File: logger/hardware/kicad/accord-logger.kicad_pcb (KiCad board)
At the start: 2 copper layers, 120 x 80 mm, 31 parts, among them J1 Board connector 14-way, J5 SD breakout 6-way, Q5 IPD50P04P4L-11, Q6 2N3904, Q7 2N3904, U1 RaspberryPi_Pico_W, U6 LM2678T-5.0

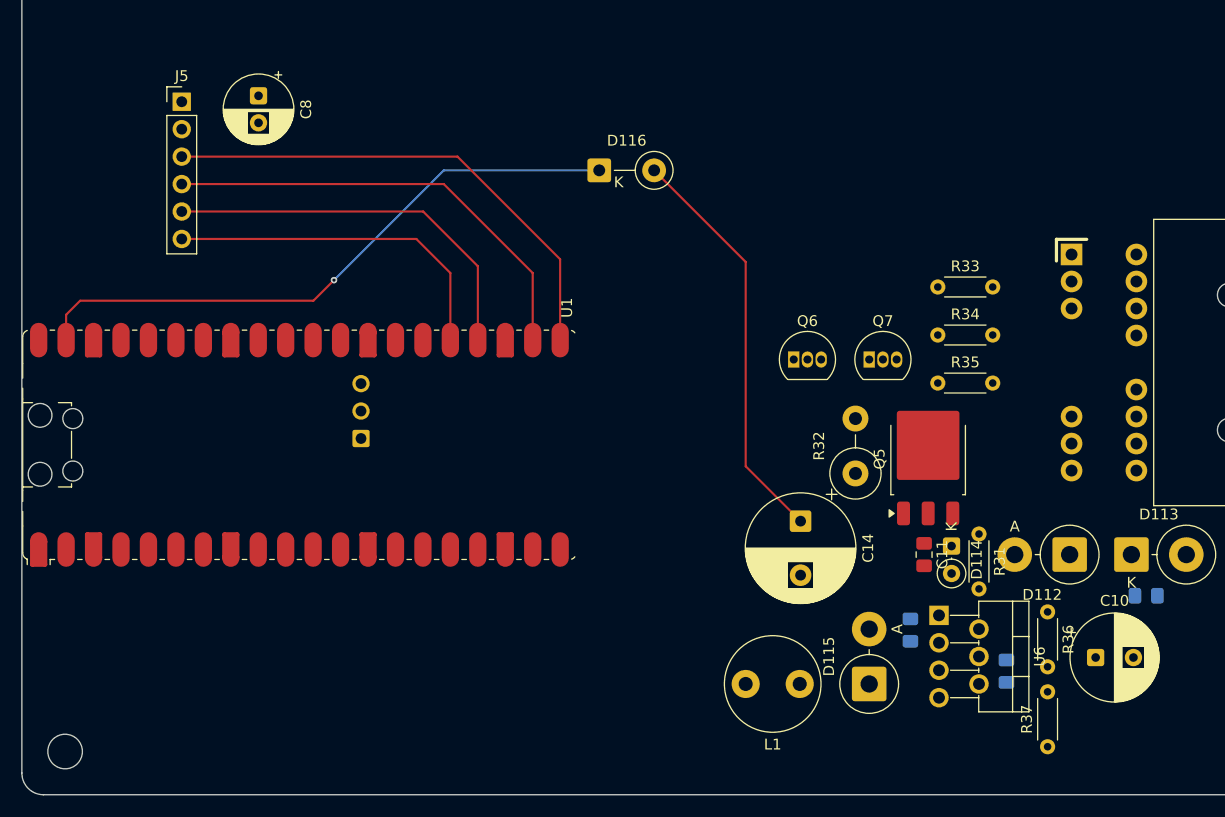
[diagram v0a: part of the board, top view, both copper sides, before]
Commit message: layout: Pico turned antenna-to-edge, buck loop tightened
Owner changes after the first review:
- U1 rotated 0 deg: antenna end at the bottom board edge, USB end inboard
  with its cable keepout clear to the top edge.
- Buck rearranged around U6 (now 90 deg): hot loop CIN -> VIN -> SW ->
  catch diode -> CIN- is 12.7 + 10.1 + 11.4 mm (was 11.1 + 9.1 + 24.6;
  keyless 9.5 + 6.5 + 22.9). L1 to SW 7.1 mm (was 14.4).
- R32/C14 courtyard overlap fixed.

Review findings (scratch-copy DRC; schematic parity: only the 39 timer
parts not yet pulled in):
- J5's drawn SD-module courtyard (B side, x 110-126, y 119-136) covers
  the Pico antenna keepout from behind.
- H4 hole edge reaches ~0.4 mm into the RF keepout; NPTH, no copper.
- C11 (CIB, VIN ceramic) is 14 mm from U6.2 (keyless C16: 3.2 mm);
  C12 (CBOOST) 12.7/10.5 mm from U6.1/U6.3 (keyless 6.2/8.7).
- C14 output bulk is ~30 mm from L1's output pad.
- 0.5 mm dangling P12 stub on B.Cu at D113.1.
- Silkscreen overlaps only otherwise.

Claude-Session-ID: 42dd0e33-28b5-4936-847e-9c2e1d2488fa
Co-Authored-By: Claude Opus 5.5 <noreply@anthropic.com>
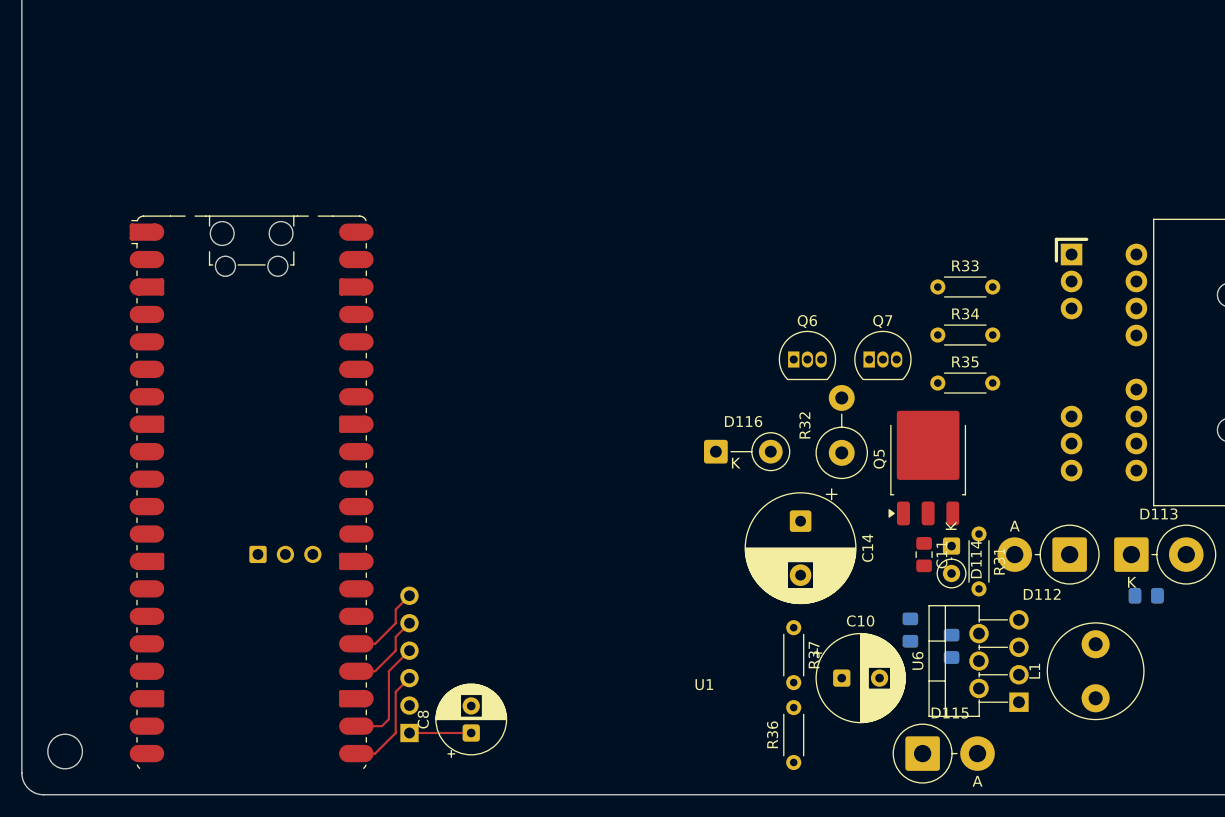
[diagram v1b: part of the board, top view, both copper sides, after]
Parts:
- J5: moved to B.Cu
- moved C8 62.2 mm to (130.2, 134.0), turned to 90 degrees
- moved J5 62.1 mm to (124.5, 134.0)
- moved D116 28.2 mm to (152.8, 108.0)
- moved L1 27.4 mm to (188.0, 130.8), turned to 90 degrees
- moved R36 27.3 mm to (160.0, 136.7), turned to 90 degrees
- moved R37 25.9 mm to (160.0, 124.2), turned to -90 degrees
- moved C10 23.6 mm to (164.5, 128.9)
- moved U6 10.9 mm to (180.9, 131.1), turned to 90 degrees
- moved D115 8.12 mm to (171.9, 135.9), turned to 0 degrees
- moved U1 6.27 mm to (109.9, 111.8), turned to 0 degrees
- moved C13 5.58 mm to (174.6, 126.0), turned to -90 degrees
- moved R32 2.29 mm to (164.5, 108.1)
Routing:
- net /VSYS: track 57.2 -> 0.00 mm, vias 1 -> 0
- net /B5: track 38.1 -> 0.00 mm
- net /SD_MISO: track 46.4 -> 10.0 mm
- net /SD_CS: track 42.1 -> 10.4 mm
- net /SD_SCK: track 36.3 -> 7.50 mm
- net /SD_MOSI: track 32.4 -> 7.50 mm
- net /P3V3_SW: track 0.00 -> 5.72 mm

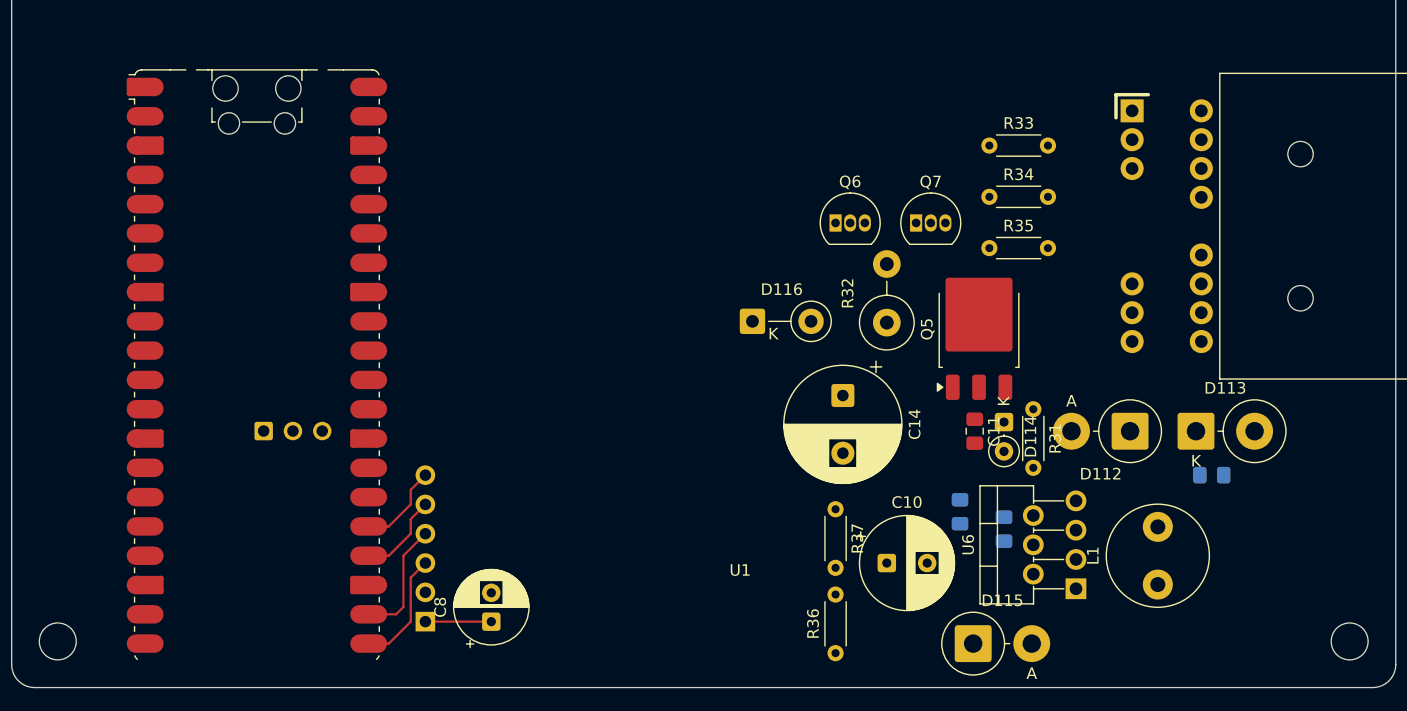
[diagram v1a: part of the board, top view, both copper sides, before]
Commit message: layout: buck bypass caps at U6, SD module beside the antenna
Owner fixes after the second review (scratch-copy DRC; only the 39 timer
parts are missing from schematic parity):
- C11 (VIN ceramic) 2.6/5.7 mm from U6.2/U6.4, was 14 (keyless 3.2).
- C12 (boost) 2.7/2.7 mm from U6.1/U6.3, was 12.7/10.5.
- C13 2.5/2.6 mm from U6.6/U6.4.
- C14 10.8 mm from L1's output, was ~30; C14- to D115 A 21.9 mm.
- J5's SD-module outline moved off the Pico antenna (now x 120.8-137.1,
  3.8 mm clear of the antenna keepout).
- Dangling P12 stub removed.
Hot loop unchanged (12.7 + 10.1 + 11.4 mm). Remaining: H4 hole edge in
the RF keepout (NPTH; use nylon hardware), silkscreen tidy-up.

Claude-Session-ID: 42dd0e33-28b5-4936-847e-9c2e1d2488fa
Co-Authored-By: Claude Opus 5.5 <noreply@anthropic.com>
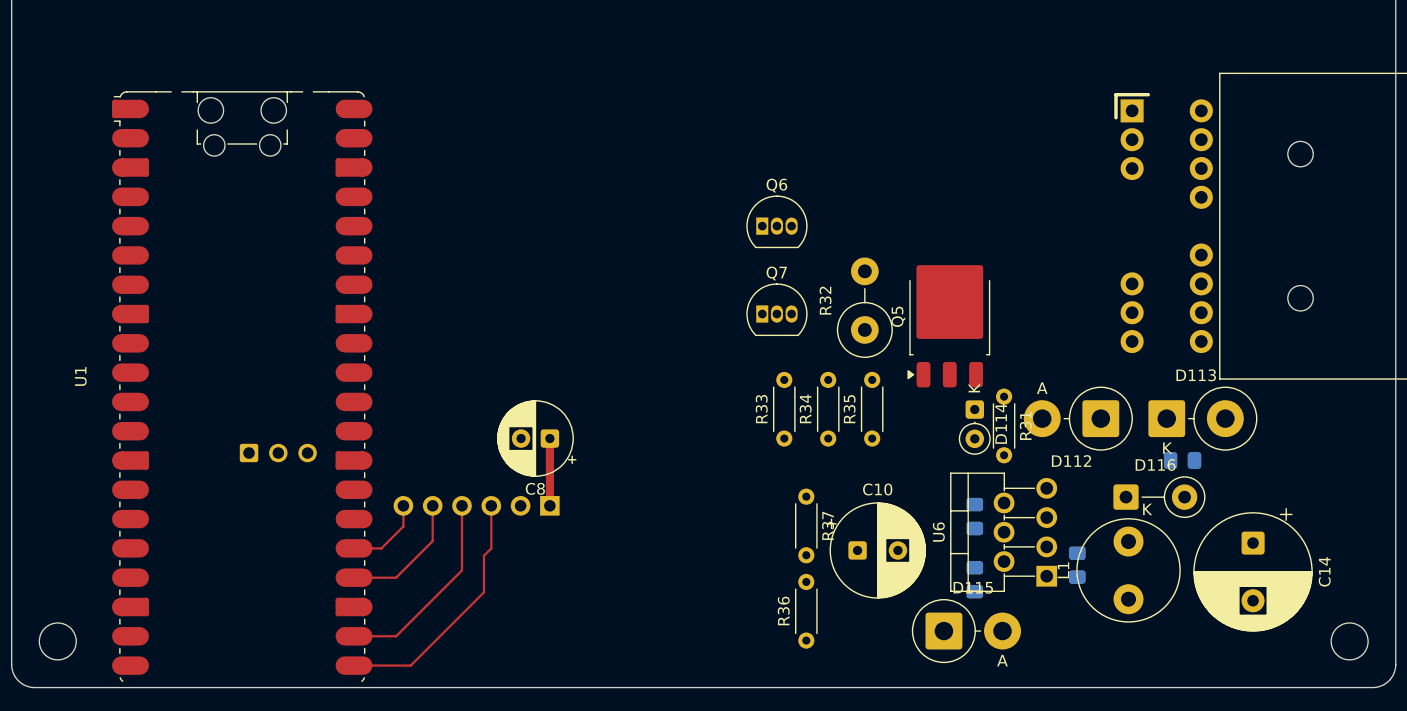
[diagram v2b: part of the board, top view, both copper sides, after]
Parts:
- C11: moved to B.Cu
- moved C14 37.8 mm to (196.2, 127.2)
- moved D116 35.8 mm to (185.2, 123.2)
- moved R33 31.0 mm to (155.6, 118.1), turned to 90 degrees
- moved R34 25.2 mm to (159.4, 118.1), turned to 90 degrees
- moved R35 19.4 mm to (163.2, 118.1), turned to 90 degrees
- moved C8 16.7 mm to (135.3, 118.1), turned to 180 degrees
- moved Q7 15.5 mm to (153.7, 107.3)
- moved J5 14.7 mm to (135.3, 123.9), turned to 90 degrees
- moved C11 12.9 mm to (172.1, 130.4)
- moved C12 11.2 mm to (181.0, 129.1), turned to 90 degrees
- moved Q6 6.36 mm to (153.7, 99.7)
- moved L1 2.84 mm to (185.4, 132.0)
- moved C9 2.84 mm to (190.1, 120.0)
- moved C10 2.76 mm to (161.9, 127.8)
- moved C13 2.76 mm to (172.1, 124.9)
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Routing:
- net /SD_MISO: track 10.0 -> 21.7 mm
- net /SD_CS: track 10.4 -> 17.3 mm
- net /SD_SCK: track 7.50 -> 11.2 mm
- net /SD_MOSI: track 7.50 -> 6.85 mm

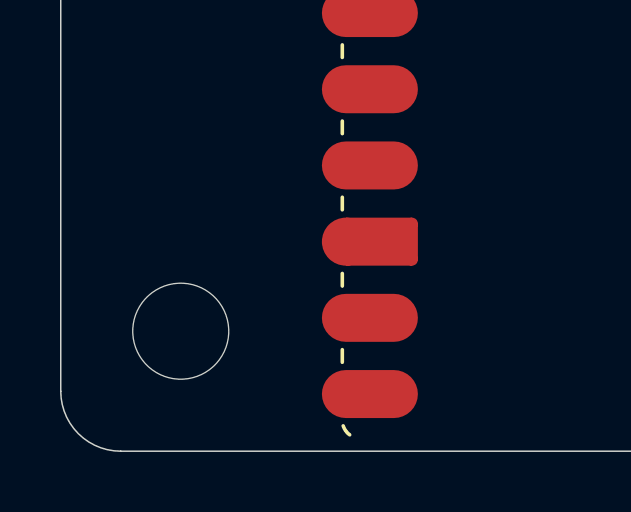
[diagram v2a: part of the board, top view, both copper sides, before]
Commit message: layout: H4 moved 1.08 mm inboard, clear of the Pico RF keepout
Hole edge now at y 136.22, the keepout starts at 136.76. H4 is no longer
4 mm from the bottom edge like H2 (134.62 vs 135.70).

Claude-Session-ID: 42dd0e33-28b5-4936-847e-9c2e1d2488fa
Co-Authored-By: Claude Opus 5.5 <noreply@anthropic.com>
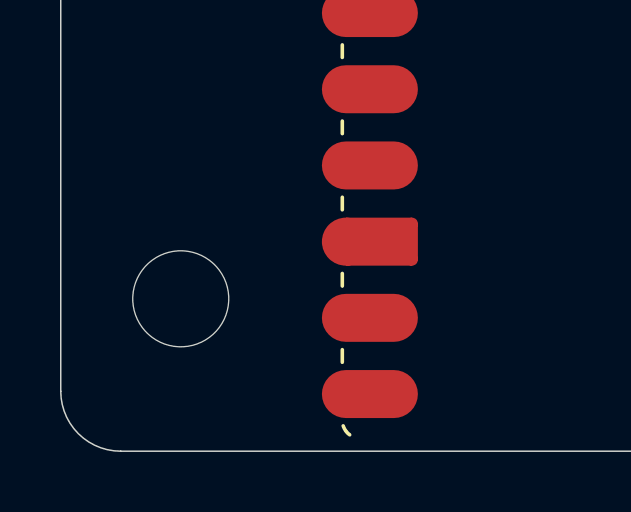
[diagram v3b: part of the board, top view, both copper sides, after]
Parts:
- moved H4 1.08 mm to (92.6, 134.6)
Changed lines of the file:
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@@
 	(footprint "MountingHole:MountingHole_3.2mm_M3"
 		(layer "F.Cu")
-		(at 92.59 135.7 -90)
+		(at 92.59 134.62 -90)
 		(descr "Mounting Hole 3.2mm, M3, no annular, generated by kicad-footprint-generator mountinghole.py")
 		(tags "mountinghole M3")

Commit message: layout: timer batch imported (39 parts, off the board edge, unplaced)
a5_supply, hold, clock and cutoff came in with "Update PCB from Schematic";
they sit to the right of the outline, x 215-270 mm. No placed footprint moved.

Claude-Session-ID: 42dd0e33-28b5-4936-847e-9c2e1d2488fa
Co-Authored-By: Claude Opus 5.5 <noreply@anthropic.com>
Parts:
- added C15: 33uF/16V, Capacitor_Tantalum_SMD:CP_EIA-7343-31_Kemet-D_HandSolder, F.Cu at (222.9, 68.6)
- added C16: 10nF, Capacitor_SMD:C_0805_2012Metric_Pad1.18x1.45mm_HandSolder, F.Cu at (247.3, 66.7)
- added C17: 100nF, Capacitor_SMD:C_0805_2012Metric_Pad1.18x1.45mm_HandSolder, F.Cu at (247.3, 71.2)
- added C18: 100nF, Capacitor_SMD:C_0805_2012Metric_Pad1.18x1.45mm_HandSolder, F.Cu at (247.3, 75.7)
- added C19: 100nF, Capacitor_SMD:C_0805_2012Metric_Pad1.18x1.45mm_HandSolder, F.Cu at (247.3, 80.0)
- added C20: 100nF, Capacitor_SMD:C_0805_2012Metric_Pad1.18x1.45mm_HandSolder, F.Cu at (247.3, 84.5)
- added C21: 100nF, Capacitor_SMD:C_0805_2012Metric_Pad1.18x1.45mm_HandSolder, F.Cu at (247.3, 88.7)
- added C22: 100nF, Capacitor_SMD:C_0805_2012Metric_Pad1.18x1.45mm_HandSolder, F.Cu at (247.3, 93.2)
- added C23: 100nF, Capacitor_SMD:C_0805_2012Metric_Pad1.18x1.45mm_HandSolder, F.Cu at (247.3, 97.7)
- added C4: 4.7uF/50V, Capacitor_SMD:C_1210_3225Metric_Pad1.33x2.70mm_HandSolder, F.Cu at (261.6, 72.4)
- added C5: 4.7uF/50V, Capacitor_SMD:C_1210_3225Metric_Pad1.33x2.70mm_HandSolder, F.Cu at (261.6, 78.7)
- added C6: 4.7uF/50V, Capacitor_SMD:C_1210_3225Metric_Pad1.33x2.70mm_HandSolder, F.Cu at (261.6, 85.1)
- added C7: 100nF, Capacitor_SMD:C_0805_2012Metric_Pad1.18x1.45mm_HandSolder, F.Cu at (247.3, 62.2)
- added D111: BZX55C22, Diode_THT:D_DO-35_SOD27_P2.54mm_Vertical_KathodeUp, F.Cu at (235.6, 85.1)
- added JP1: HOLD link, Connector_PinHeader_2.54mm:PinHeader_1x02_P2.54mm_Vertical, F.Cu at (217.2, 76.8)
- added Q8: BSS138P, Package_TO_SOT_SMD:SOT-23, F.Cu at (270.2, 74.6)
- added Q9: MMBT3904, Package_TO_SOT_SMD:SOT-23, F.Cu at (270.2, 81.4)
- added R22: 820R, Resistor_SMD:R_1206_3216Metric_Pad1.30x1.75mm_HandSolder, F.Cu at (267.0, 55.9)
- added R28: 47k, Resistor_SMD:R_0805_2012Metric_Pad1.20x1.40mm_HandSolder, F.Cu at (252.0, 62.2)
- added R29: 1k, Resistor_SMD:R_0805_2012Metric_Pad1.20x1.40mm_HandSolder, F.Cu at (252.1, 66.6)
- added R38: 1k, Resistor_SMD:R_0805_2012Metric_Pad1.20x1.40mm_HandSolder, F.Cu at (252.1, 71.1)
- added R39: 0R, Resistor_SMD:R_1206_3216Metric_Pad1.30x1.75mm_HandSolder, F.Cu at (267.0, 61.0)
- added R40: 0R, Resistor_SMD:R_1206_3216Metric_Pad1.30x1.75mm_HandSolder, F.Cu at (267.0, 66.0)
- added R41: 100k, Resistor_SMD:R_0805_2012Metric_Pad1.20x1.40mm_HandSolder, F.Cu at (252.1, 75.5)
- added R42: 1k, Resistor_SMD:R_0805_2012Metric_Pad1.20x1.40mm_HandSolder, F.Cu at (252.0, 79.7)
- added R43: 100k, Resistor_SMD:R_0805_2012Metric_Pad1.20x1.40mm_HandSolder, F.Cu at (252.0, 84.1)
- added R44: 47k, Resistor_SMD:R_0805_2012Metric_Pad1.20x1.40mm_HandSolder, F.Cu at (252.0, 88.3)
- added R45: 100k, Resistor_SMD:R_0805_2012Metric_Pad1.20x1.40mm_HandSolder, F.Cu at (252.1, 92.7)
- added R46: 100k, Resistor_SMD:R_0805_2012Metric_Pad1.20x1.40mm_HandSolder, F.Cu at (252.0, 97.2)
- added U10: CD74HC4060M96, Package_SO:SOIC-16_3.9x9.9mm_P1.27mm, F.Cu at (215.8, 46.4)
- added U11: CD74HC4020M96, Package_SO:SOIC-16_3.9x9.9mm_P1.27mm, F.Cu at (224.3, 46.4)
- added U12: CD4011BM96, Package_SO:SOIC-14_3.9x8.7mm_P1.27mm, F.Cu at (232.6, 45.7)
- added U13: CD4071BM96, Package_SO:SOIC-14_3.9x8.7mm_P1.27mm, F.Cu at (241.0, 45.7)
- added U14: CD4093BM96, Package_SO:SOIC-14_3.9x8.7mm_P1.27mm, F.Cu at (249.5, 45.7)
- added U4: TPS70950QDBVRQ1, Package_TO_SOT_SMD:SOT-23-5_HandSoldering, F.Cu at (225.4, 83.2)
- added U5: TPS3839K50DBZR, Package_TO_SOT_SMD:SOT-23, F.Cu at (270.2, 88.0)
- added U7: OV-7604-C7-32.768KHZ-20PPM-TA-QC, accord-logger:Oscillator_SMD_MicroCrystal_OV-7604-C7_SON-4_3.2x1.5mm, F.Cu at (233.0, 68.6)
- added U8: 74AHC1G17GV, Package_TO_SOT_SMD:SOT-353_SC-70-5_Handsoldering, F.Cu at (228.0, 76.2)
- added U9: SN74LVC1G97DBVR, Package_TO_SOT_SMD:SOT-23-6_Handsoldering, F.Cu at (236.3, 77.8)
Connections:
- U1 pad 26: unconnected-(U1-GPIO20-Pad26) -> /RTC_SDA
- U1 pad 27: unconnected-(U1-GPIO21-Pad27) -> /RTC_SCL
- U1 pad 29: unconnected-(U1-GPIO22-Pad29) -> /RTC_INT

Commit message: layout: timer batch removed from the board for now
Back to the power block, Pico, SD header, J1 and the four holes.

Claude-Session-ID: 42dd0e33-28b5-4936-847e-9c2e1d2488fa
Co-Authored-By: Claude Opus 5.5 <noreply@anthropic.com>
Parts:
- removed C15: 33uF/16V, Capacitor_Tantalum_SMD:CP_EIA-7343-31_Kemet-D_HandSolder
- removed C16: 10nF, Capacitor_SMD:C_0805_2012Metric_Pad1.18x1.45mm_HandSolder
- removed C17, C18, C19, C20, C21, C22, C23, C7: 100nF, Capacitor_SMD:C_0805_2012Metric_Pad1.18x1.45mm_HandSolder
- removed C4, C5, C6: 4.7uF/50V, Capacitor_SMD:C_1210_3225Metric_Pad1.33x2.70mm_HandSolder
- removed D111: BZX55C22, Diode_THT:D_DO-35_SOD27_P2.54mm_Vertical_KathodeUp
- removed JP1: HOLD link, Connector_PinHeader_2.54mm:PinHeader_1x02_P2.54mm_Vertical
- removed Q8: BSS138P, Package_TO_SOT_SMD:SOT-23
- removed Q9: MMBT3904, Package_TO_SOT_SMD:SOT-23
- removed R22: 820R, Resistor_SMD:R_1206_3216Metric_Pad1.30x1.75mm_HandSolder
- removed R28, R44: 47k, Resistor_SMD:R_0805_2012Metric_Pad1.20x1.40mm_HandSolder
- removed R29, R38, R42: 1k, Resistor_SMD:R_0805_2012Metric_Pad1.20x1.40mm_HandSolder
- removed R39, R40: 0R, Resistor_SMD:R_1206_3216Metric_Pad1.30x1.75mm_HandSolder
- removed R41, R43, R45, R46: 100k, Resistor_SMD:R_0805_2012Metric_Pad1.20x1.40mm_HandSolder
- removed U10: CD74HC4060M96, Package_SO:SOIC-16_3.9x9.9mm_P1.27mm
- removed U11: CD74HC4020M96, Package_SO:SOIC-16_3.9x9.9mm_P1.27mm
- removed U12: CD4011BM96, Package_SO:SOIC-14_3.9x8.7mm_P1.27mm
- removed U13: CD4071BM96, Package_SO:SOIC-14_3.9x8.7mm_P1.27mm
- removed U14: CD4093BM96, Package_SO:SOIC-14_3.9x8.7mm_P1.27mm
- removed U4: TPS70950QDBVRQ1, Package_TO_SOT_SMD:SOT-23-5_HandSoldering
- removed U5: TPS3839K50DBZR, Package_TO_SOT_SMD:SOT-23
- removed U7: OV-7604-C7-32.768KHZ-20PPM-TA-QC, accord-logger:Oscillator_SMD_MicroCrystal_OV-7604-C7_SON-4_3.2x1.5mm
- removed U8: 74AHC1G17GV, Package_TO_SOT_SMD:SOT-353_SC-70-5_Handsoldering
- removed U9: SN74LVC1G97DBVR, Package_TO_SOT_SMD:SOT-23-6_Handsoldering
